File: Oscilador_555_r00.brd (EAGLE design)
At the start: 49.7 x 49.8 mm, 8 parts, among them IC1 LM555

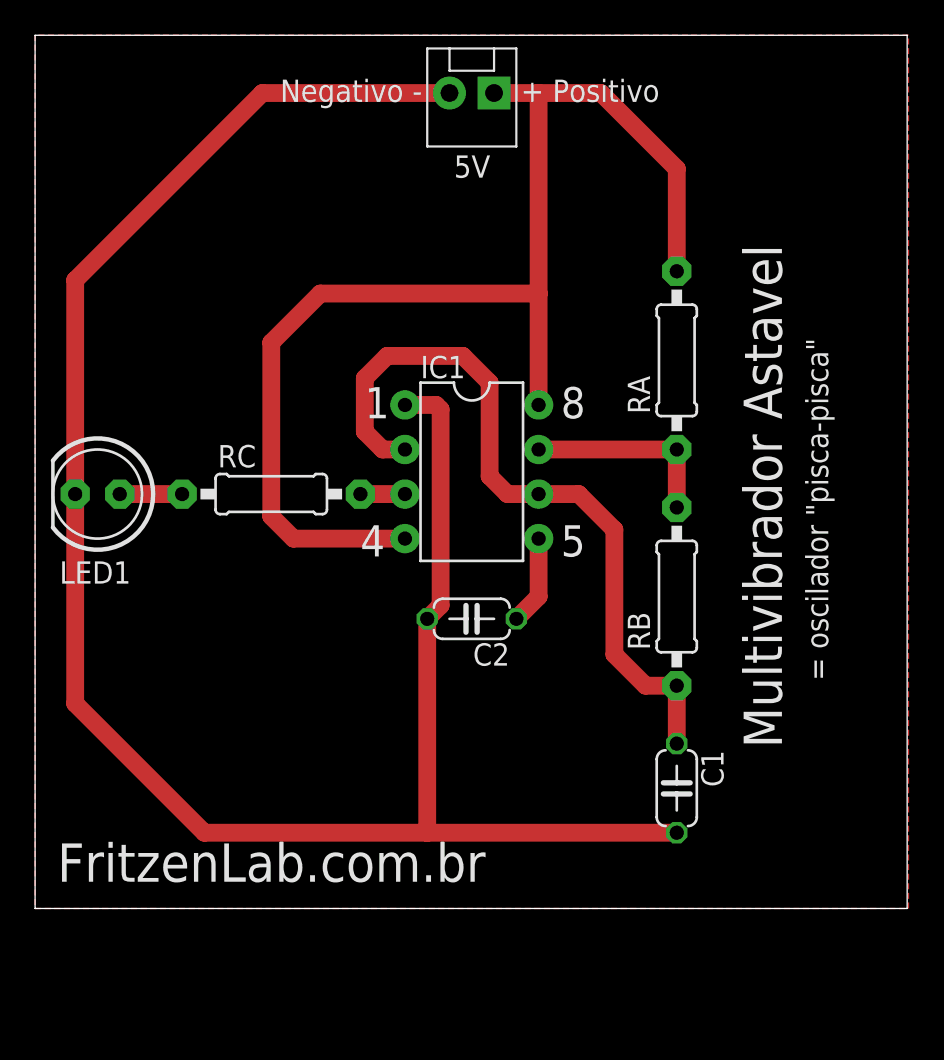
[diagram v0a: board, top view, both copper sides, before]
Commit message: Primeira revisao e arquivos zip para producao
Primeira revisão (estética e para adicionar conector KRE 5mm); criado
Gerber para producao da PCI
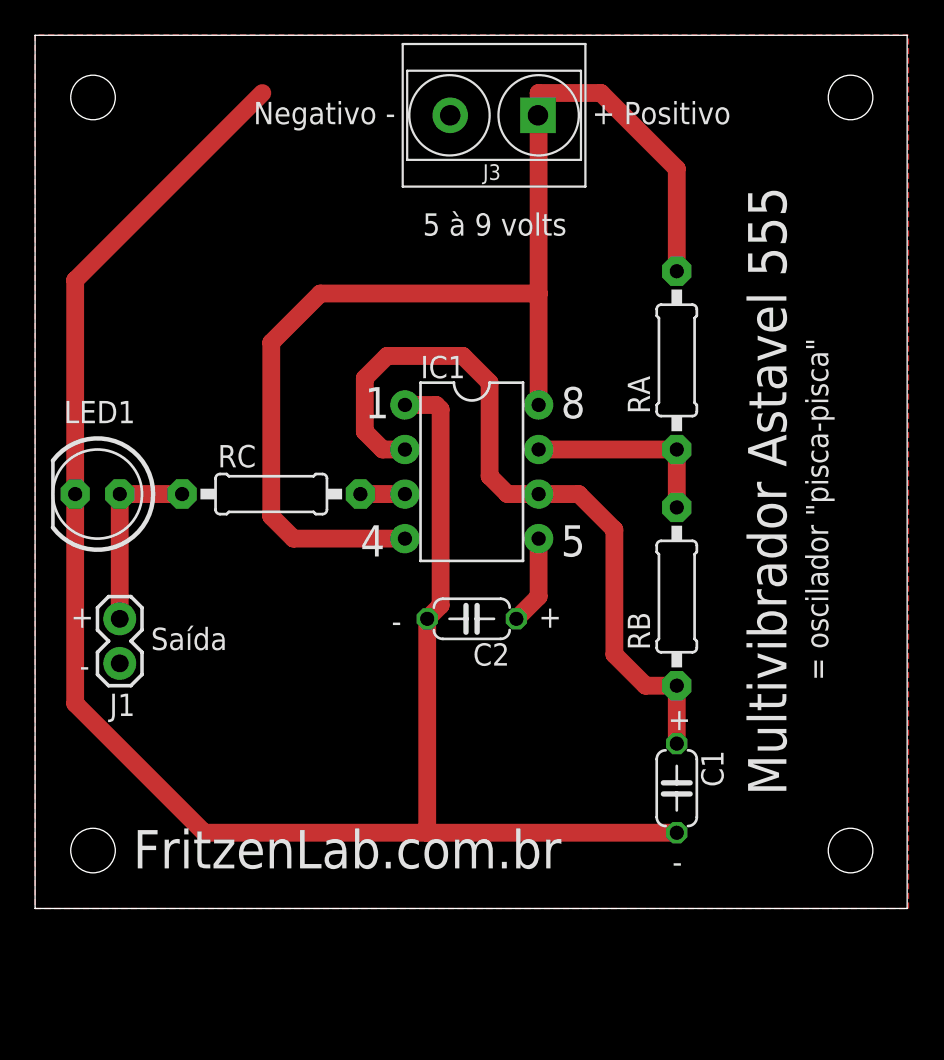
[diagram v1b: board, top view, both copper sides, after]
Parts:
- added J3: GSL009-5.0-02P-12, Seeed-OPL-Connector:H2-5.0-10.5X8.0MM
- J1: device SparkFun-Connectors:MOLEX-1X2 -> SparkFun-Connectors:1X02
- moved J1 36.8 mm to (4.83, 16.5), turned to 270 degrees
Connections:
- net GND: now also J3.2
- net N$3: now also J1.1
- net VCC: now also J3.1; no longer J1.1
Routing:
- net GND: track 113.8 -> 103.1 mm
- net N$3: track 3.56 -> 10.7 mm
- net VCC: track 70.3 -> 67.8 mm
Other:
- board text added: "+"
- board text added: "-"
- board text added: "5 à 9 volts"
- board text added: "Multivibrador Astavel 555"
- board text added: "Saída"
- board text removed: "5V"
- board text removed: "Multivibrador Astavel"
